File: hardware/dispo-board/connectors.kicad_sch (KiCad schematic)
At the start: 1 part, among them J1 USB_B_Micro

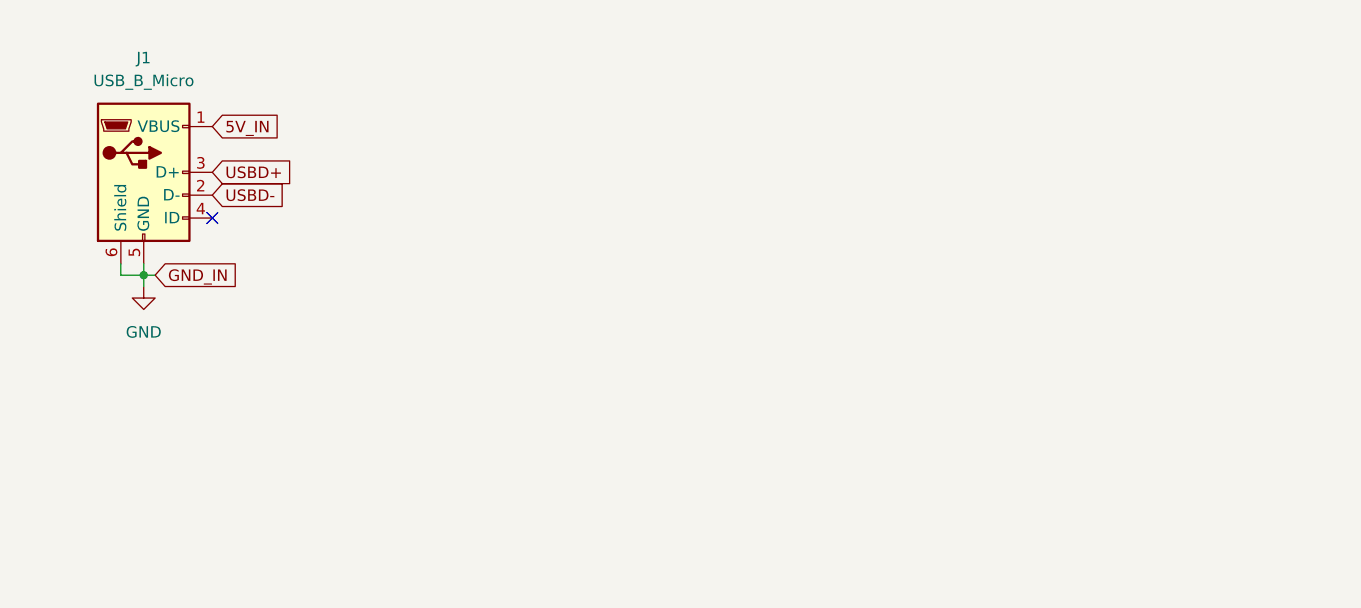
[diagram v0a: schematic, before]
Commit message: add decoupling caps, connectors, audio, minor corrections in report
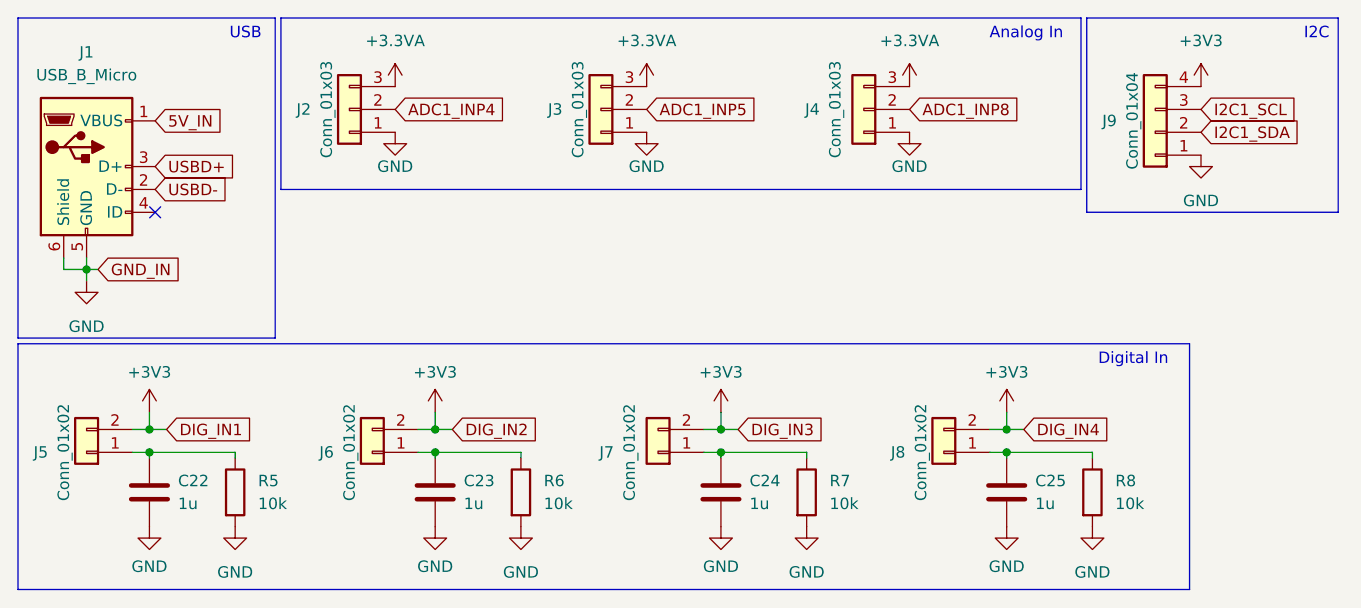
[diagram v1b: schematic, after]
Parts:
- added C22, C23, C24, C25: 1u, symbol Device:C
- added J2, J3, J4: Conn_01x03, MyFootprints:solder_pad_1x3_D2.00mm, symbol Connector_Generic:Conn_01x03
- added J5, J6, J7, J8: Conn_01x02, MyFootprints:solder_pad_1x2_D2.00mm, symbol Connector_Generic:Conn_01x02
- added J9: Conn_01x04, Connector_PinHeader_2.54mm:PinHeader_1x04_P2.54mm_Vertical, symbol Connector_Generic:Conn_01x04
- added R5, R6, R7, R8: 10k, symbol Device:R
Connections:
- net GND: now also C22.2, C23.2, C24.2, C25.2, J2.1 (Pin_1), J3.1 (Pin_1), J4.1 (Pin_1), J9.1 (Pin_1), R5.2, R6.2, R7.2, R8.2
- new net: C22.1, J5.1 (Pin_1), R5.1
- new net: C24.1, J7.1 (Pin_1), R7.1
- new net: C23.1, J6.1 (Pin_1), R6.1
- new net: C25.1, J8.1 (Pin_1), R8.1
- new net +3.3VA: J2.3 (Pin_3), J3.3 (Pin_3), J4.3 (Pin_3)
- new net +3V3: J5.2 (Pin_2), J6.2 (Pin_2), J7.2 (Pin_2), J8.2 (Pin_2), J9.4 (Pin_4)
- new net ADC1_INP4: J2.2 (Pin_2)
- new net ADC1_INP5: J3.2 (Pin_2)
- new net ADC1_INP8: J4.2 (Pin_2)
- new net I2C1_SCL: J9.3 (Pin_3)
- new net I2C1_SDA: J9.2 (Pin_2)
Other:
- note added: "Analog In"
- note added: "Digital In"
- note added: "I2C"
- note added: "USB"
- moved on the sheet: J1

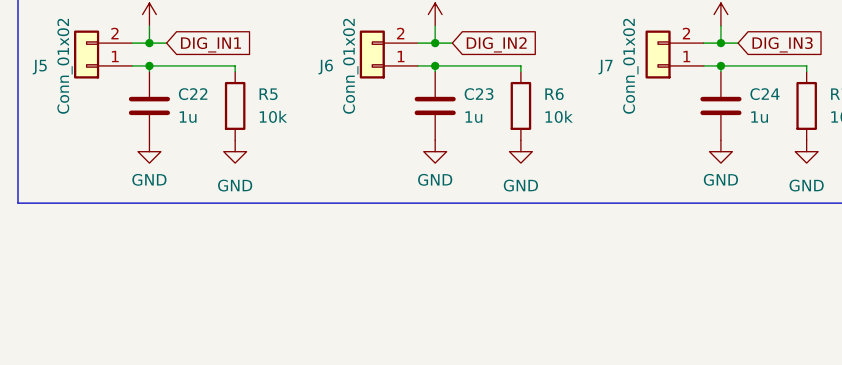
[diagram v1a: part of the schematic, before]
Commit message: added analog frontend
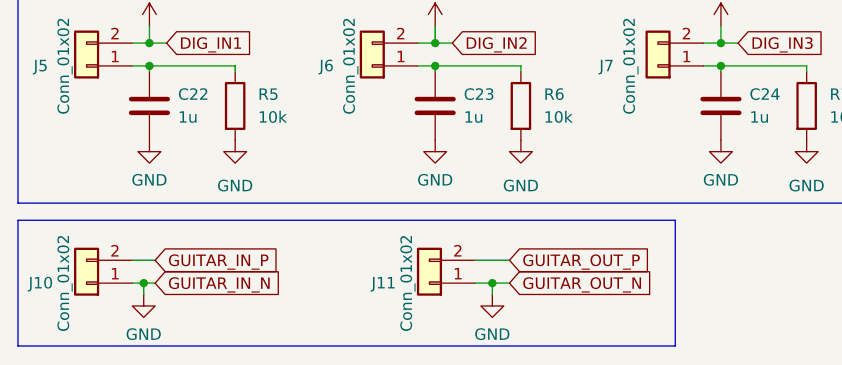
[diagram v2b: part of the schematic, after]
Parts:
- added J10, J11: Conn_01x02, MyFootprints:solder_pad_1x2_D2.00mm, symbol Connector_Generic:Conn_01x02
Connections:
- net GND: now also J10.1 (Pin_1), J11.1 (Pin_1)
- new net GUITAR_IN_P: J10.2 (Pin_2)
- new net GUITAR_OUT_P: J11.2 (Pin_2)
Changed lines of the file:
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@@
   (junction (at 33.655 64.135) (diameter 0) (color 0 0 0 0)
   )
+  (junction (at 33.02 90.805) (diameter 0) (color 0 0 0 0)
+  )
   (junction (at 65.405 64.135) (diameter 0) (color 0 0 0 0)
   )
   (junction (at 26.67 46.355) (diameter 0) (color 0 0 0 0)
+  )
+  (junction (at 71.755 90.805) (diameter 0) (color 0 0 0 0)
   )
   (junction (at 97.155 66.675) (diameter 0) (color 0 0 0 0)
@@
     (stroke (width 0) (type default))
   )
+  (wire (pts (xy 71.755 90.805) (xy 73.66 90.805))
+    (stroke (width 0) (type default))
+  )
   (wire (pts (xy 31.75 66.675) (xy 33.655 66.675))
     (stroke (width 0) (type default))
@@
     (stroke (width 0) (type default))
   )
+  (wire (pts (xy 71.755 90.805) (xy 71.755 92.075))
+    (stroke (width 0) (type default))
+  )
   (wire (pts (xy 24.13 46.355) (xy 26.67 46.355))
     (stroke (width 0) (type default))
@@
     (stroke (width 0) (type default))
   )
+  (wire (pts (xy 31.75 90.805) (xy 33.02 90.805))
+    (stroke (width 0) (type default))
+  )
   (wire (pts (xy 26.67 46.355) (xy 26.67 47.625))
     (stroke (width 0) (type default))
@@
     (stroke (width 0) (type default))
   )
+  (wire (pts (xy 69.85 88.265) (xy 73.66 88.265))
+    (stroke (width 0) (type default))
+  )
   (wire (pts (xy 128.905 66.675) (xy 128.905 67.31))
     (stroke (width 0) (type default))
@@
     (stroke (width 0) (type default))
   )
+  (wire (pts (xy 33.02 90.805) (xy 33.02 92.075))
+    (stroke (width 0) (type default))
+  )
   (wire (pts (xy 97.155 64.135) (xy 99.06 64.135))
     (stroke (width 0) (type default))
@@
     (stroke (width 0) (type default))
   )
+  (wire (pts (xy 31.75 88.265) (xy 34.29 88.265))
+    (stroke (width 0) (type default))
+  )
   (wire (pts (xy 63.5 66.675) (xy 65.405 66.675))
     (stroke (width 0) (type default))
@@
     (stroke (width 0) (type default))
   )
+  (wire (pts (xy 33.02 90.805) (xy 34.29 90.805))
+    (stroke (width 0) (type default))
+  )
   (wire (pts (xy 128.905 66.675) (xy 138.43 66.675))
     (stroke (width 0) (type default))
@@
     (stroke (width 0) (type default))
   )
+  (wire (pts (xy 69.85 90.805) (xy 71.755 90.805))
+    (stroke (width 0) (type default))
+  )
   (wire (pts (xy 95.25 66.675) (xy 97.155 66.675))
     (stroke (width 0) (type default))
@@
   )
   (rectangle (start 19.05 18.415) (end 47.625 53.975)
+    (stroke (width 0) (type default))
+    (fill (type none))
+  )
+  (rectangle (start 19.05 83.82) (end 92.075 97.79)
     (stroke (width 0) (type default))
     (fill (type none))
@@
     )
   )
+  (global_label "GUITAR_IN_N" (shape input) (at 34.29 90.805 0) (fields_autoplaced)
+    (effects (font (size 1.27 1.27)) (justify left))
+    (property "Intersheetrefs" "${INTERSHEET_REFS}" (at 49.0077 90.805 0)
+      (effects (font (size 1.27 1.27)) (justify left) hide)
+    )
+  )
+  (global_label "GUITAR_OUT_N" (shape input) (at 73.66 90.805 0) (fields_autoplaced)
+    (effects (font (size 1.27 1.27)) (justify left))
+    (property "Intersheetrefs" "${INTERSHEET_REFS}" (at 90.071 90.805 0)
+      (effects (font (size 1.27 1.27)) (justify left) hide)
+    )
+  )
   (global_label "ADC1_INP8" (shape input) (at 118.11 28.575 0) (fields_autoplaced)
     (effects (font (size 1.27 1.27)) (justify left))
@@
     )
   )
+  (global_label "GUITAR_OUT_P" (shape input) (at 73.66 88.265 0) (fields_autoplaced)
+    (effects (font (size 1.27 1.27)) (justify left))
+    (property "Intersheetrefs" "${INTERSHEET_REFS}" (at 90.0105 88.265 0)
+      (effects (font (size 1.27 1.27)) (justify left) hide)
+    )
+  )
   (global_label "ADC1_INP5" (shape input) (at 88.9 28.575 0) (fields_autoplaced)
     (effects (font (size 1.27 1.27)) (justify left))
@@
     )
   )
+  (global_label "GUITAR_IN_P" (shape input) (at 34.29 88.265 0) (fields_autoplaced)
+    (effects (font (size 1.27 1.27)) (justify left))
+    (property "Intersheetrefs" "${INTERSHEET_REFS}" (at 48.9472 88.265 0)
+      (effects (font (size 1.27 1.27)) (justify left) hide)
+    )
+  )
   (global_label "DIG_IN4" (shape input) (at 130.81 64.135 0) (fields_autoplaced)
     (effects (font (size 1.27 1.27)) (justify left))
@@
     )
   )
+  (symbol (lib_id "Connector_Generic:Conn_01x02") (at 26.67 90.805 180) (unit 1)
+    (in_bom yes) (on_board yes) (dnp no)
+    (property "Reference" "J10" (at 21.59 90.805 0)
+      (effects (font (size 1.27 1.27)))
+    )
+    (property "Value" "Conn_01x02" (at 24.13 90.805 90)
+      (effects (font (size 1.27 1.27)))
+    )
+    (property "Footprint" "MyFootprints:solder_pad_1x2_D2.00mm" (at 26.67 90.805 0)
+      (effects (font (size 1.27 1.27)) hide)
+    )
+    (property "Datasheet" "~" (at 26.67 90.805 0)
+      (effects (font (size 1.27 1.27)) hide)
+    )
+    (pin "1")
+    (pin "2")
+    (instances
+      (project "dispo-board"
+        (path "/93ea4da8-8485-4fb5-a89d-c72021d94c09/b8888756-c15f-4275-bc58-daa9bb032a86"
+          (reference "J10") (unit 1)
+        )
+      )
+    )
+  )
   (symbol (lib_id "power:GND") (at 43.18 74.93 0) (unit 1)
     (in_bom yes) (on_board yes) (dnp no) (fields_autoplaced)
@@
         (path "/93ea4da8-8485-4fb5-a89d-c72021d94c09/b8888756-c15f-4275-bc58-daa9bb032a86"
           (reference "#PWR038") (unit 1)
+        )
+      )
+    )
+  )
+  (symbol (lib_id "power:GND") (at 33.02 92.075 0) (unit 1)
+    (in_bom yes) (on_board yes) (dnp no) (fields_autoplaced)
+    (property "Reference" "#PWR067" (at 33.02 98.425 0)
+      (effects (font (size 1.27 1.27)) hide)
+    )
+    (property "Value" "GND" (at 33.02 96.52 0)
+      (effects (font (size 1.27 1.27)))
+    )
+    (property "Footprint" "" (at 33.02 92.075 0)
+      (effects (font (size 1.27 1.27)) hide)
+    )
+    (property "Datasheet" "" (at 33.02 92.075 0)
+      (effects (font (size 1.27 1.27)) hide)
+    )
+    (pin "1")
+    (instances
+      (project "dispo-board"
+        (path "/93ea4da8-8485-4fb5-a89d-c72021d94c09/b8888756-c15f-4275-bc58-daa9bb032a86"
+          (reference "#PWR067") (unit 1)
         )
       )
@@
     )
   )
+  (symbol (lib_id "Connector_Generic:Conn_01x02") (at 64.77 90.805 180) (unit 1)
+    (in_bom yes) (on_board yes) (dnp no)
+    (property "Reference" "J11" (at 59.69 90.805 0)
+      (effects (font (size 1.27 1.27)))
+    )
+    (property "Value" "Conn_01x02" (at 62.23 90.805 90)
+      (effects (font (size 1.27 1.27)))
+    )
+    (property "Footprint" "MyFootprints:solder_pad_1x2_D2.00mm" (at 64.77 90.805 0)
+      (effects (font (size 1.27 1.27)) hide)
+    )
+    (property "Datasheet" "~" (at 64.77 90.805 0)
+      (effects (font (size 1.27 1.27)) hide)
+    )
+    (pin "1")
+    (pin "2")
+    (instances
+      (project "dispo-board"
+        (path "/93ea4da8-8485-4fb5-a89d-c72021d94c09/b8888756-c15f-4275-bc58-daa9bb032a86"
+          (reference "J11") (unit 1)
+        )
+      )
+    )
+  )
   (symbol (lib_id "Connector_Generic:Conn_01x04") (at 145.415 31.115 180) (unit 1)
     (in_bom yes) (on_board yes) (dnp no)
@@
         )
       )
+    )
+  )
+  (symbol (lib_id "power:GND") (at 71.755 92.075 0) (unit 1)
+    (in_bom yes) (on_board yes) (dnp no) (fields_autoplaced)
+    (property "Reference" "#PWR068" (at 71.755 98.425 0)
+      (effects (font (size 1.27 1.27)) hide)
+    )
+    (property "Value" "GND" (at 71.755 96.52 0)
+      (effects (font (size 1.27 1.27)))
+    )
+    (property "Footprint" "" (at 71.755 92.075 0)
+      (effects (font (size 1.27 1.27)) hide)
+    )
+    (property "Datasheet" "" (at 71.755 92.075 0)
+      (effects (font (size 1.27 1.27)) hide)
+    )
+    (pin "1")
+    (instances
+      (project "dispo-board"
+        (path "/93ea4da8-8485-4fb5-a89d-c72021d94c09/b8888756-c15f-4275-bc58-daa9bb032a86"
+          (reference "#PWR068") (unit 1)
+        )
+      )

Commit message: maybe final schematic?
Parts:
- added J12, J13: Conn_01x03, MyFootprints:solder_pad_1x3_D2.00mm, symbol Connector_Generic:Conn_01x03
- added JP1, JP2: Jumper_3_Open, symbol Jumper:Jumper_3_Open
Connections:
- net GUITAR_IN_P: now also JP1.2 (C)
- net GUITAR_OUT_P: now also JP2.2 (C)
- new net GUITAR_IN_switch: J12.2 (Pin_2), JP1.1 (A)
- new net GUITAR_IN_µC: J12.3 (Pin_3), JP1.3 (B)
- new net GUITAR_OUT_switch: J13.2 (Pin_2), JP2.1 (A)
- new net GUITAR_OUT_µC: J13.3 (Pin_3), JP2.3 (B)
- new net GUITAR_bypass: J12.1 (Pin_1), J13.1 (Pin_1)
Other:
- note added: "Audio IN/OUT"
- note added: "Bypass switch"
- note added: "Selection Switch/Direct"
- moved on the sheet: J10, J11
